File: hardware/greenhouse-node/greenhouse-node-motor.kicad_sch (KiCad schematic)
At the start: 24 parts, among them J7 Conn_01x02_Male, Q10 2N2222A, Q2 2N2222A, Q3 2N2222A, Q4 IRF9530N, Q5 IRF530N, Q6 D44H8, Q7 IRF9530N, Q8 IRF530N, Q9 2N2222A, U4 L7810

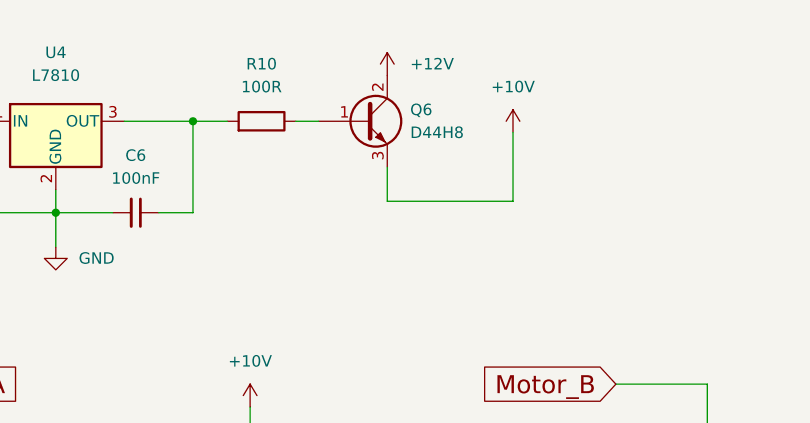
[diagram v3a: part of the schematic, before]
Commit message: Changed power BJT for FET
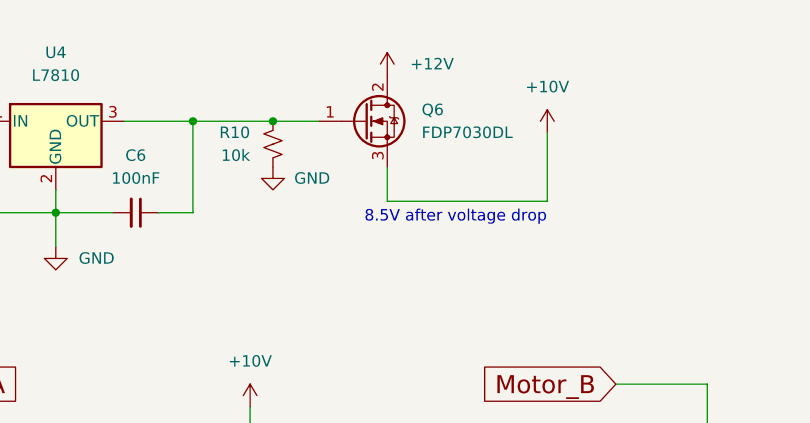
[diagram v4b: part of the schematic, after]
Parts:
- removed Q6: D44H8, Package_TO_SOT_THT:TO-220-3_Horizontal_TabDown, symbol Transistor_BJT:BD911
- removed R10: 100R, Resistor_THT:R_Axial_DIN0204_L3.6mm_D1.6mm_P5.08mm_Horizontal, symbol Device:R
- added Q6: FDP7030DL, Package_TO_SOT_THT:TO-220-3_Horizontal_TabDown, symbol Transistor_FET:IRF540N
- added R10: 10k, Resistor_THT:R_Axial_DIN0204_L3.6mm_D1.6mm_P7.62mm_Horizontal, symbol Device:R_Small_US
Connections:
- net +10V: now also Q6.3 (S)
- net +12V: now also Q6.2 (D)
- net GND: now also R10.1
- net at C6.1, U4.3 (OUT): now also Q6.1 (G), R10.2
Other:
- note added: "8.5V after voltage drop"
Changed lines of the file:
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@@
   (junction (at 88.9 119.38) (diameter 0) (color 0 0 0 0)
   )
+  (junction (at 114.3 58.42) (diameter 0) (color 0 0 0 0)
+  )
   (junction (at 134.62 92.71) (diameter 0) (color 0 0 0 0)
   )
@@
     (stroke (width 0) (type default) (color 0 0 0 0))
   )
-  (wire (pts (xy 116.84 58.42) (xy 119.38 58.42))
-    (stroke (width 0) (type default) (color 0 0 0 0))
-  )
   (wire (pts (xy 90.17 66.04) (xy 90.17 68.58))
     (stroke (width 0) (type default) (color 0 0 0 0))
@@
     (stroke (width 0) (type default) (color 0 0 0 0))
   )
+  (wire (pts (xy 114.3 58.42) (xy 119.38 58.42))
+    (stroke (width 0) (type default) (color 0 0 0 0))
+  )
   (wire (pts (xy 125.73 92.71) (xy 134.62 92.71))
     (stroke (width 0) (type default) (color 0 0 0 0))
   )
-  (wire (pts (xy 140.97 67.31) (xy 140.97 59.69))
+  (wire (pts (xy 144.78 67.31) (xy 144.78 59.69))
     (stroke (width 0) (type default) (color 0 0 0 0))
   )
@@
     (stroke (width 0) (type default) (color 0 0 0 0))
   )
-  (wire (pts (xy 105.41 58.42) (xy 109.22 58.42))
+  (wire (pts (xy 105.41 58.42) (xy 114.3 58.42))
     (stroke (width 0) (type default) (color 0 0 0 0))
   )
@@
     (stroke (width 0) (type default) (color 0 0 0 0))
   )
-  (wire (pts (xy 127 67.31) (xy 140.97 67.31))
+  (wire (pts (xy 127 67.31) (xy 144.78 67.31))
     (stroke (width 0) (type default) (color 0 0 0 0))
   )
@@
   (wire (pts (xy 111.76 92.71) (xy 125.73 92.71))
     (stroke (width 0) (type default) (color 0 0 0 0))
+  )
+  (text "8.5V after voltage drop" (at 124.46 69.85 0)
+    (effects (font (size 1.27 1.27)) (justify left bottom))
   )
   (label "Motor_1" (at 196.85 106.68 0)
@@
   (symbol (lib_id "power:+12V") (at 127 53.34 0) (unit 1)
     (in_bom yes) (on_board yes) (fields_autoplaced)
-    (property "Reference" "#PWR026" (id 0) (at 127 57.15 0)
+    (property "Reference" "#PWR027" (id 0) (at 127 57.15 0)
       (effects (font (size 1.27 1.27)) hide)
     )
@@
   (symbol (lib_id "power:GND") (at 228.6 120.65 0) (unit 1)
     (in_bom yes) (on_board yes) (fields_autoplaced)
-    (property "Reference" "#PWR030" (id 0) (at 228.6 127 0)
+    (property "Reference" "#PWR031" (id 0) (at 228.6 127 0)
       (effects (font (size 1.27 1.27)) hide)
     )
@@
     (pin "3")
   )
+  (symbol (lib_id "Transistor_FET:IRF540N") (at 124.46 58.42 0) (unit 1)
+    (in_bom yes) (on_board yes) (fields_autoplaced)
+    (property "Reference" "Q6" (id 0) (at 130.81 57.1499 0)
+      (effects (font (size 1.27 1.27)) (justify left))
+    )
+    (property "Value" "FDP7030DL" (id 1) (at 130.81 59.6899 0)
+      (effects (font (size 1.27 1.27)) (justify left))
+    )
+    (property "Footprint" "Package_TO_SOT_THT:TO-220-3_Horizontal_TabDown" (id 2) (at 130.81 60.325 0)
+      (effects (font (size 1.27 1.27) italic) (justify left) hide)
+    )
+    (property "Datasheet" "www.farnell.com/datasheets/245431.pdf" (id 3) (at 124.46 58.42 0)
+      (effects (font (size 1.27 1.27)) (justify left) hide)
+    )
+    (pin "1")
+    (pin "2")
+    (pin "3")
+  )
   (symbol (lib_id "Device:R_Small_US") (at 152.4 96.52 0) (mirror x) (unit 1)
     (in_bom yes) (on_board yes) (fields_autoplaced)
@@
   (symbol (lib_id "power:GND") (at 152.4 113.03 0) (mirror y) (unit 1)
     (in_bom yes) (on_board yes)
-    (property "Reference" "#PWR029" (id 0) (at 152.4 119.38 0)
+    (property "Reference" "#PWR030" (id 0) (at 152.4 119.38 0)
       (effects (font (size 1.27 1.27)) hide)
     )
@@
     (pin "3")
   )
-  (symbol (lib_id "power:+10V") (at 140.97 59.69 0) (unit 1)
-    (in_bom yes) (on_board yes) (fields_autoplaced)
-    (property "Reference" "#PWR028" (id 0) (at 140.97 63.5 0)
-      (effects (font (size 1.27 1.27)) hide)
-    )
-    (property "Value" "+10V" (id 1) (at 140.97 54.61 0))
-    (property "Footprint" "" (id 2) (at 140.97 59.69 0)
-      (effects (font (size 1.27 1.27)) hide)
-    )
-    (property "Datasheet" "" (id 3) (at 140.97 59.69 0)
+  (symbol (lib_id "power:+10V") (at 144.78 59.69 0) (unit 1)
+    (in_bom yes) (on_board yes) (fields_autoplaced)
+    (property "Reference" "#PWR029" (id 0) (at 144.78 63.5 0)
+      (effects (font (size 1.27 1.27)) hide)
+    )
+    (property "Value" "+10V" (id 1) (at 144.78 54.61 0))
+    (property "Footprint" "" (id 2) (at 144.78 59.69 0)
+      (effects (font (size 1.27 1.27)) hide)
+    )
+    (property "Datasheet" "" (id 3) (at 144.78 59.69 0)
       (effects (font (size 1.27 1.27)) hide)
     )
@@
   (symbol (lib_id "power:GND") (at 134.62 135.89 0) (mirror y) (unit 1)
     (in_bom yes) (on_board yes)
-    (property "Reference" "#PWR027" (id 0) (at 134.62 142.24 0)
+    (property "Reference" "#PWR028" (id 0) (at 134.62 142.24 0)
       (effects (font (size 1.27 1.27)) hide)
     )
@@
     (pin "1")
   )
-  (symbol (lib_id "Device:R") (at 113.03 58.42 270) (mirror x) (unit 1)
-    (in_bom yes) (on_board yes) (fields_autoplaced)
-    (property "Reference" "R10" (id 0) (at 113.03 52.07 90))
-    (property "Value" "100R" (id 1) (at 113.03 54.61 90))
-    (property "Footprint" "Resistor_THT:R_Axial_DIN0204_L3.6mm_D1.6mm_P5.08mm_Horizontal" (id 2) (at 113.03 60.198 90)
-      (effects (font (size 1.27 1.27)) hide)
-    )
-    (property "Datasheet" "~" (id 3) (at 113.03 58.42 0)
-      (effects (font (size 1.27 1.27)) hide)
-    )
-    (pin "1")
-    (pin "2")
-  )
   (symbol (lib_id "power:GND") (at 88.9 135.89 0) (unit 1)
     (in_bom yes) (on_board yes) (fields_autoplaced)
@@
     )
     (pin "1")
+  )
+  (symbol (lib_id "Device:R_Small_US") (at 114.3 60.96 0) (mirror x) (unit 1)
+    (in_bom yes) (on_board yes) (fields_autoplaced)
+    (property "Reference" "R10" (id 0) (at 111.76 59.6899 0)
+      (effects (font (size 1.27 1.27)) (justify right))
+    )
+    (property "Value" "10k" (id 1) (at 111.76 62.2299 0)
+      (effects (font (size 1.27 1.27)) (justify right))
+    )
+    (property "Footprint" "Resistor_THT:R_Axial_DIN0204_L3.6mm_D1.6mm_P7.62mm_Horizontal" (id 2) (at 114.3 60.96 0)
+      (effects (font (size 1.27 1.27)) hide)
+    )
+    (property "Datasheet" "~" (id 3) (at 114.3 60.96 0)
+      (effects (font (size 1.27 1.27)) hide)
+    )
+    (pin "1")
+    (pin "2")
   )
   (symbol (lib_id "Device:R_Small_US") (at 162.56 96.52 180) (unit 1)
@@
     (pin "2")
   )
-  (symbol (lib_id "Transistor_BJT:BD911") (at 124.46 58.42 0) (unit 1)
-    (in_bom yes) (on_board yes) (fields_autoplaced)
-    (property "Reference" "Q6" (id 0) (at 129.54 57.1499 0)
-      (effects (font (size 1.27 1.27)) (justify left))
-    )
-    (property "Value" "D44H8" (id 1) (at 129.54 59.6899 0)
-      (effects (font (size 1.27 1.27)) (justify left))
-    )
-    (property "Footprint" "Package_TO_SOT_THT:TO-220-3_Horizontal_TabDown" (id 2) (at 130.81 60.325 0)
-      (effects (font (size 1.27 1.27) italic) (justify left) hide)
-    )
-    (property "Datasheet" "http://www.st.com/internet/com/TECHNICAL_RESOURCES/TECHNICAL_LITERATURE/DATASHEET/CD00001277.pdf" (id 3) (at 124.46 58.42 0)
-      (effects (font (size 1.27 1.27)) (justify left) hide)
-    )
-    (pin "1")
-    (pin "2")
-    (pin "3")
-  )
   (symbol (lib_id "Transistor_FET:IRF540N") (at 128.27 119.38 0) (mirror y) (unit 1)
     (in_bom yes) (on_board yes) (fields_autoplaced)
@@
     (pin "3")
   )
+  (symbol (lib_id "power:GND") (at 114.3 63.5 0) (mirror y) (unit 1)
+    (in_bom yes) (on_board yes)
+    (property "Reference" "#PWR026" (id 0) (at 114.3 69.85 0)
+      (effects (font (size 1.27 1.27)) hide)
+    )
+    (property "Value" "GND" (id 1) (at 120.65 64.77 0)
+      (effects (font (size 1.27 1.27)) (justify left))
+    )
+    (property "Footprint" "" (id 2) (at 114.3 63.5 0)
+      (effects (font (size 1.27 1.27)) hide)
+    )
+    (property "Datasheet" "" (id 3) (at 114.3 63.5 0)
+      (effects (font (size 1.27 1.27)) hide)
+    )
+    (pin "1")
+  )
   (symbol (lib_id "Nick:2N2222A") (at 86.36 130.81 0) (unit 1)
